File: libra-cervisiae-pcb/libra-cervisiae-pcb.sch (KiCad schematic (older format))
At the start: 20 parts, among them CN1 CP2102-BREAKOUT, CN2 HX711_BREAKOUT, J1 Wort Temp, J2 Ambient Temp, J3 Load Cells, SW1 Reset, SW2 Flash, U1 ESP32-WROOM-32, U2 VREG

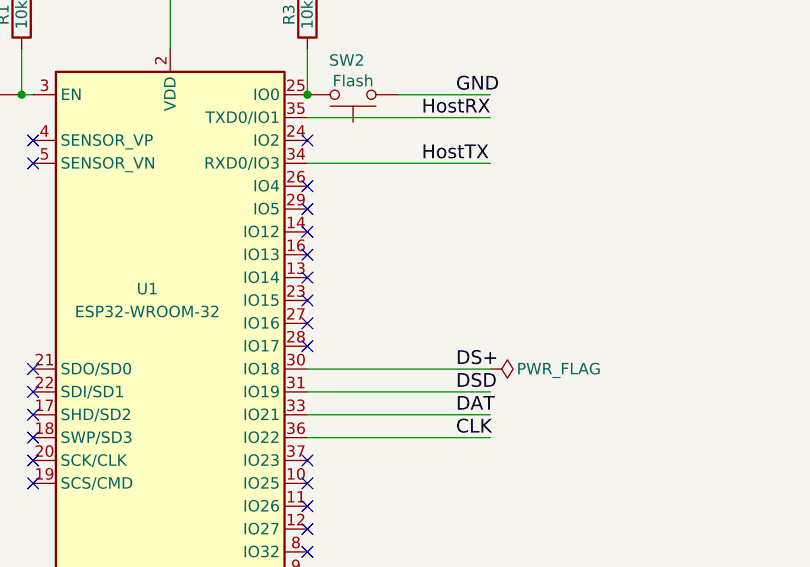
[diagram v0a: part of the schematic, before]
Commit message: Add a Hotspot button to restart into hotspot mode
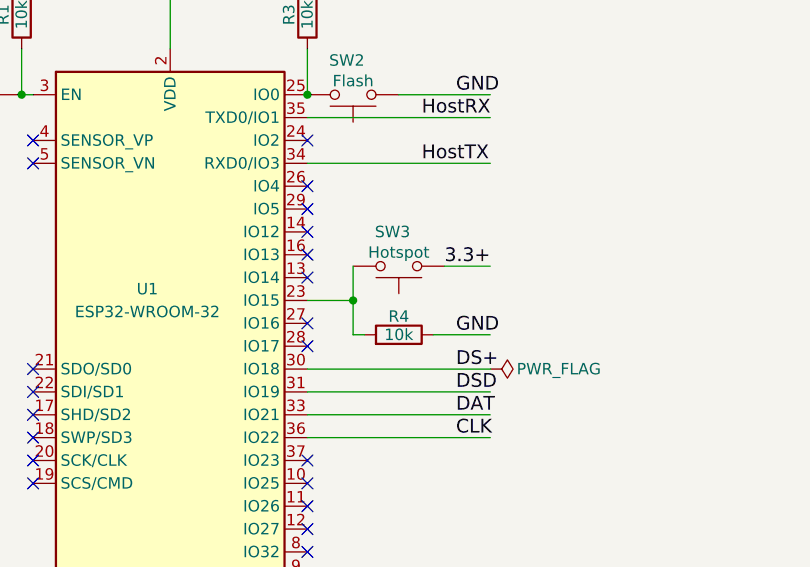
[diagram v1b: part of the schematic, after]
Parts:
- added R4: 10k, Resistor_SMD:R_0805_2012Metric, symbol Device:R
- added SW3: Hotspot, 4x3_SWITCH:4x3_Switch, symbol Switch:SW_Push
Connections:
- wire segments 99 -> 105
- no-connect marks 28 -> 27
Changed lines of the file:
@@
 Text Label 6350 1300 0    60   ~ 0
 GND
-Connection ~ 5700 1300
 Wire Wire Line
 	5700 2700 6500 2700
@@
 NoConn ~ 5700 2400
 NoConn ~ 5700 2300
-NoConn ~ 5700 2200
 NoConn ~ 5700 2100
 NoConn ~ 5700 2000
@@
 Wire Wire Line
 	3650 1300 4050 1300
+$Comp
+L Switch:SW_Push SW3
+U 1 1 5D785ABF
+P 6100 2050
+F 0 "SW3" H 6050 1900 50  0000 L CNN
+F 1 "Hotspot" H 6100 1990 50  0000 C CNN
+F 2 "4x3_SWITCH:4x3_Switch" H 6100 2250 50  0001 C CNN
+F 3 "" H 6100 2250 50  0001 C CNN
+	1    6100 2050
+	-1   0    0    1
+$EndComp
+Connection ~ 5700 1300
+Wire Wire Line
+	5700 2200 5900 2200
+Wire Wire Line
+	5900 2200 5900 2050
+Wire Wire Line
+	6300 2050 6500 2050
+Text Label 6300 2050 0    60   ~ 0
+3.3+
+Wire Wire Line
+	5900 2200 5900 2350
+Connection ~ 5900 2200
+$Comp
+L Device:R R4
+U 1 1 5D79D805
+P 6100 2350
+F 0 "R4" V 6180 2350 50  0000 C CNN
+F 1 "10k" V 6100 2350 50  0000 C CNN
+F 2 "Resistor_SMD:R_0805_2012Metric" V 6030 2350 50  0001 C CNN
+F 3 "" H 6100 2350 50  0001 C CNN
+	1    6100 2350
+	0    1    -1   0
+$EndComp
+Wire Wire Line
+	5900 2350 5950 2350
+Wire Wire Line
+	6250 2350 6500 2350
+Text Label 6350 2350 0    60   ~ 0
+GND
 $EndSCHEMATC

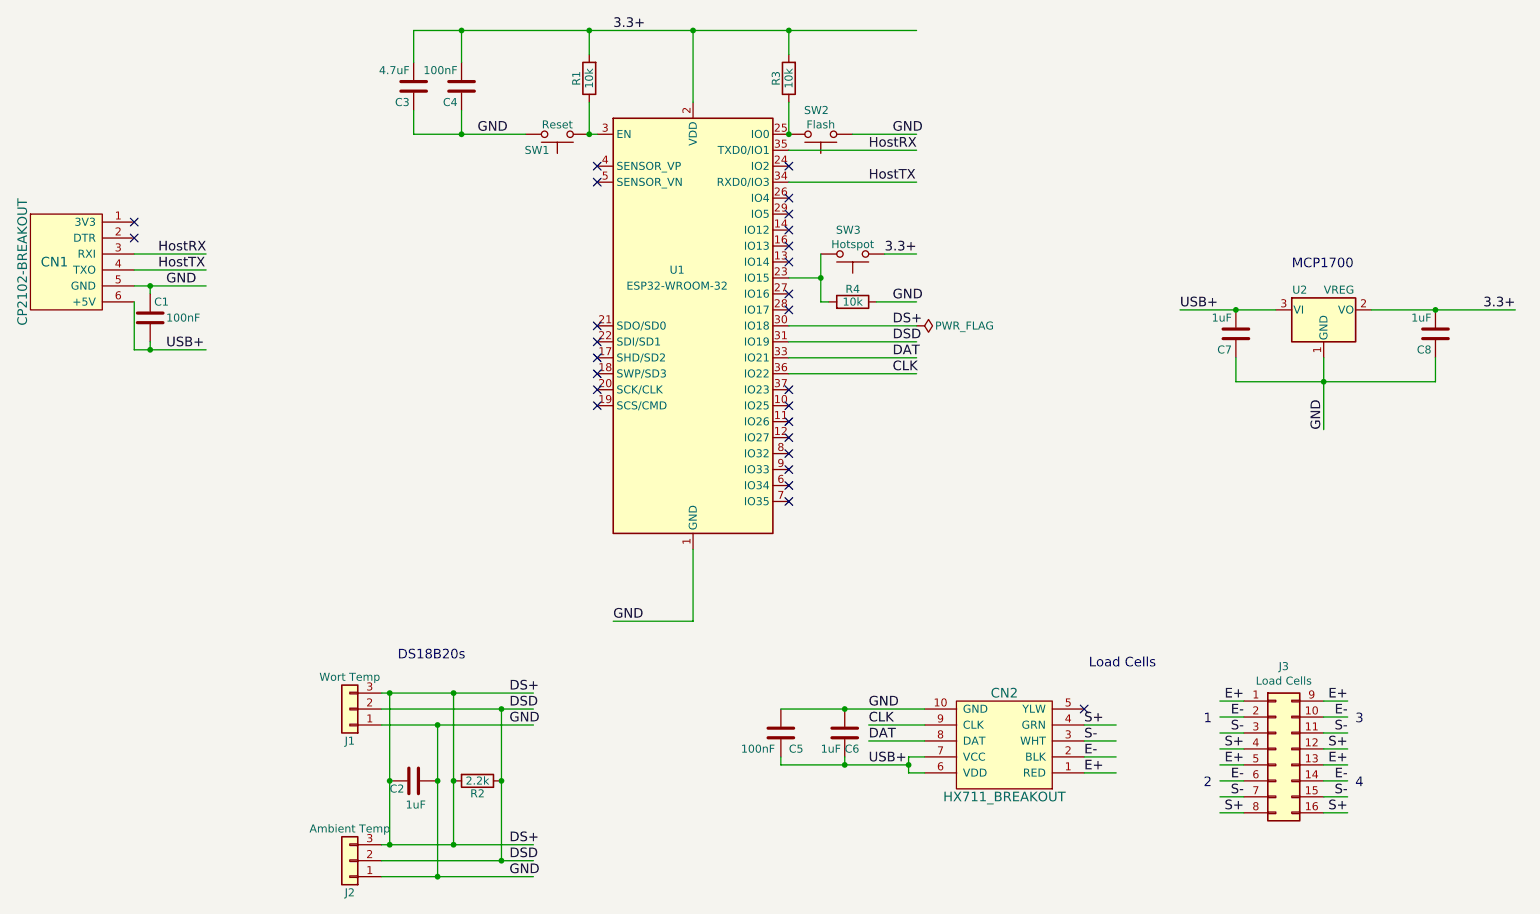
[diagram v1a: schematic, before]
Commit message: Redo board to DP8049 size
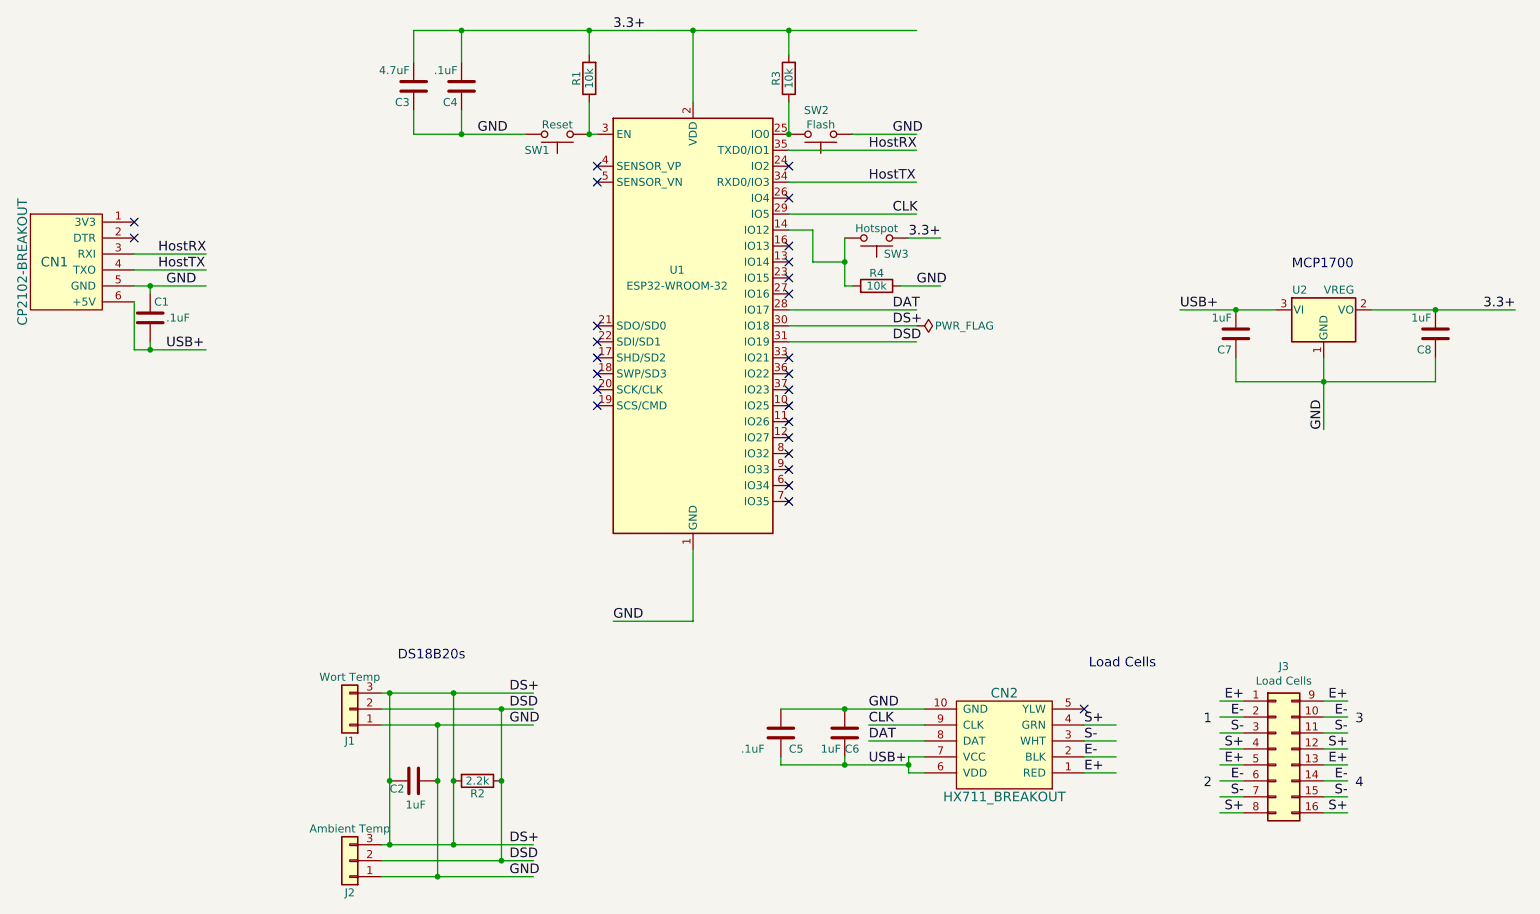
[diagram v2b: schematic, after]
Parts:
- C1, C4, C5: value 100nF -> .1uF
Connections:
- wire segments 105 -> 107
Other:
- moved on the sheet: R4, SW3
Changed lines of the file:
@@
 P 1700 2450
 F 0 "C1" H 1725 2550 50  0000 L CNN
-F 1 "100nF" H 1800 2450 50  0000 L CNN
+F 1 ".1uF" H 1800 2450 50  0000 L CNN
 F 2 "Capacitor_SMD:C_0805_2012Metric" H 1738 2300 50  0001 C CNN
 F 3 "" H 1700 2450 50  0001 C CNN
@@
 P 3650 1000
 F 0 "C4" H 3675 1100 50  0000 L CNN
-F 1 "100nF" H 3675 900 50  0000 L CNN
+F 1 ".1uF" H 3675 900 50  0000 L CNN
 F 2 "Capacitor_SMD:C_0805_2012Metric" H 3688 850 50  0001 C CNN
 F 3 "" H 3650 1000 50  0001 C CNN
@@
 P 5650 5050
 F 0 "C5" H 5700 4950 50  0000 L CNN
-F 1 "100nF" H 5400 4950 50  0000 L CNN
+F 1 ".1uF" H 5400 4950 50  0000 L CNN
 F 2 "Capacitor_SMD:C_0805_2012Metric" H 5688 4900 50  0001 C CNN
 F 3 "" H 5650 5050 50  0001 C CNN
@@
 GND
 Wire Wire Line
-	5700 2700 6500 2700
-Wire Wire Line
-	5700 2800 6500 2800
-Text Label 6350 2800 0    60   ~ 0
+	5700 2400 6500 2400
+Wire Wire Line
+	5700 1800 6500 1800
+Text Label 6350 1800 0    60   ~ 0
 CLK
-Text Label 6350 2700 0    60   ~ 0
+Text Label 6350 2400 0    60   ~ 0
 DAT
 Wire Wire Line
@@
 NoConn ~ 5700 3000
 NoConn ~ 5700 2900
-NoConn ~ 5700 2400
 NoConn ~ 5700 2300
 NoConn ~ 5700 2100
 NoConn ~ 5700 2000
-NoConn ~ 5700 1900
-NoConn ~ 5700 1800
 NoConn ~ 5700 1700
 NoConn ~ 5700 1500
@@
 Wire Wire Line
 	3650 1300 4050 1300
+Wire Wire Line
+	5850 2100 6050 2100
+Wire Wire Line
+	6050 2100 6050 1950
+Wire Wire Line
+	6450 1950 6650 1950
+Text Label 6450 1950 0    60   ~ 0
+3.3+
+Wire Wire Line
+	6050 2100 6050 2250
+Connection ~ 6050 2100
+$Comp
+L Device:R R4
+U 1 1 5D79D805
+P 6250 2250
+F 0 "R4" V 6330 2250 50  0000 C CNN
+F 1 "10k" V 6250 2250 50  0000 C CNN
+F 2 "Resistor_SMD:R_0805_2012Metric" V 6180 2250 50  0001 C CNN
+F 3 "" H 6250 2250 50  0001 C CNN
+	1    6250 2250
+	0    1    -1   0
+$EndComp
+Wire Wire Line
+	6050 2250 6100 2250
+Wire Wire Line
+	6400 2250 6650 2250
+Text Label 6500 2250 0    60   ~ 0
+GND
 $Comp
 L Switch:SW_Push SW3
 U 1 1 5D785ABF
-P 6100 2050
-F 0 "SW3" H 6050 1900 50  0000 L CNN
-F 1 "Hotspot" H 6100 1990 50  0000 C CNN
-F 2 "4x3_SWITCH:4x3_Switch" H 6100 2250 50  0001 C CNN
-F 3 "" H 6100 2250 50  0001 C CNN
-	1    6100 2050
-	-1   0    0    1
-$EndComp
+P 6250 1950
+F 0 "SW3" H 6050 2050 50  0000 L CNN
+F 1 "Hotspot" H 6250 1890 50  0000 C CNN
+F 2 "4x3_SWITCH:4x3_Switch" H 6250 2150 50  0001 C CNN
+F 3 "" H 6250 2150 50  0001 C CNN
+	1    6250 1950
+	-1   0    0    1
+$EndComp
+NoConn ~ 5700 2200
 Connection ~ 5700 1300
 Wire Wire Line
-	5700 2200 5900 2200
-Wire Wire Line
-	5900 2200 5900 2050
-Wire Wire Line
-	6300 2050 6500 2050
-Text Label 6300 2050 0    60   ~ 0
-3.3+
-Wire Wire Line
-	5900 2200 5900 2350
-Connection ~ 5900 2200
-$Comp
-L Device:R R4
-U 1 1 5D79D805
-P 6100 2350
-F 0 "R4" V 6180 2350 50  0000 C CNN
-F 1 "10k" V 6100 2350 50  0000 C CNN
-F 2 "Resistor_SMD:R_0805_2012Metric" V 6030 2350 50  0001 C CNN
-F 3 "" H 6100 2350 50  0001 C CNN
-	1    6100 2350
-	0    1    -1   0
-$EndComp
-Wire Wire Line
-	5900 2350 5950 2350
-Wire Wire Line
-	6250 2350 6500 2350
-Text Label 6350 2350 0    60   ~ 0
-GND
+	5700 1900 5850 1900
+Wire Wire Line
+	5850 1900 5850 2100
+NoConn ~ 5700 2700
+NoConn ~ 5700 2800
 $EndSCHEMATC
